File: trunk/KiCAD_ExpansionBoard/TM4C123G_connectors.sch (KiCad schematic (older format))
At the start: 22 parts, among them J1 TI_BOOSTER_40_J1, J2 TI_BOOSTER_40_J2, J3 TI_BOOSTER_40_J3, J4 TI_BOOSTER_40_J4, P10 EB_GPIO0, P6 CAN, P7 UART1, P8 RS485, P9 UART2, Q2 TSM3457

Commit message: Eliminata R8 e collegata la piazzola P1 direttamente al pin 2 del RFM23B. Schema elettrico alla versione 0.3.3 Cretata la BOM definitiva in (TM4C123G_CommExpBoard_BOM.xlsx e TM4C123G_CommExpBoard.csv) Completato lo sbroglio del PCB con serigrafie posizionate complete di logo OHSW. PCB alla versione 0.2
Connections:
- net labels added: +5V_TLP
- net labels removed: +5V
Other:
- note removed: "BUFFERIZZA IN INGRESSO ALL'ADC--> Radc=2k5!!"
- note removed: "if order skackable 10 pins header, \nyou can remove the four I2C pins \non this header (EB_GPIO0)"
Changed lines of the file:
@@
 Sheet 3 3
 Title "TM4C123G Communication Expansion Board"
-Date "15 jul 2014"
-Rev "0.3.1"
+Date "5 aug 2014"
+Rev "0.3.3"
 Comp "Luca Buccolini, Student @ Università Politecnica delle Marche"
 Comment1 "Expansion Board for the Texas Instruments TM4C123G Launchpad "
@@
 $EndComp
 $Comp
-L GND #PWR028
+L GND #PWR026
 U 1 1 53963620
 P 2550 1250
-F 0 "#PWR028" H 2550 1250 30  0001 C CNN
+F 0 "#PWR026" H 2550 1250 30  0001 C CNN
 F 1 "GND" H 2550 1180 30  0001 C CNN
 F 2 "" H 2550 1250 60  0000 C CNN
@@
 UART2_RST
 $Comp
-L GND #PWR029
+L GND #PWR027
 U 1 1 53963AEB
 P 5500 1250
-F 0 "#PWR029" H 5500 1250 30  0001 C CNN
+F 0 "#PWR027" H 5500 1250 30  0001 C CNN
 F 1 "GND" H 5500 1180 30  0001 C CNN
 F 2 "" H 5500 1250 60  0000 C CNN
@@
 SW1
 $Comp
-L GND #PWR030
+L GND #PWR028
 U 1 1 5396B38B
 P 9050 2550
-F 0 "#PWR030" H 9050 2550 30  0001 C CNN
+F 0 "#PWR028" H 9050 2550 30  0001 C CNN
 F 1 "GND" H 9050 2480 30  0001 C CNN
 F 2 "" H 9050 2550 60  0000 C CNN
@@
 $EndComp
 $Comp
-L GND #PWR031
+L GND #PWR029
 U 1 1 5396B419
 P 8800 3950
-F 0 "#PWR031" H 8800 3950 30  0001 C CNN
+F 0 "#PWR029" H 8800 3950 30  0001 C CNN
 F 1 "GND" H 8800 3880 30  0001 C CNN
 F 2 "" H 8800 3950 60  0000 C CNN
@@
 NoConn ~ 9250 6600
 $Comp
-L GND #PWR032
+L GND #PWR030
 U 1 1 5396D342
 P 1150 7300
-F 0 "#PWR032" H 1150 7300 30  0001 C CNN
+F 0 "#PWR030" H 1150 7300 30  0001 C CNN
 F 1 "GND" H 1150 7230 30  0001 C CNN
 F 2 "" H 1150 7300 60  0000 C CNN
@@
 $EndComp
 $Comp
-L GND #PWR033
+L GND #PWR031
 U 1 1 5396DC3C
 P 1450 7300
-F 0 "#PWR033" H 1450 7300 30  0001 C CNN
+F 0 "#PWR031" H 1450 7300 30  0001 C CNN
 F 1 "GND" H 1450 7230 30  0001 C CNN
 F 2 "" H 1450 7300 60  0000 C CNN
@@
 Text HLabel 3350 3250 2    60   Input ~ 0
 RS485_B
+Text HLabel 1550 3250 2    60   Input ~ 0
+CAN_H
 Text HLabel 1550 3150 2    60   Input ~ 0
-CAN_H
-Text HLabel 1550 3250 2    60   Input ~ 0
 CAN_L
 Text HLabel 9250 4500 0    60   Output ~ 0
@@
 UART3_TX
 $Comp
-L +12V_BUS #PWR034
+L +12V_BUS #PWR032
 U 1 1 5399D0A5
 P 1150 6000
-F 0 "#PWR034" H 1150 5950 20  0001 C CNN
+F 0 "#PWR032" H 1150 5950 20  0001 C CNN
 F 1 "+12V_BUS" H 1150 6100 30  0000 C CNN
 F 2 "" H 1150 6000 60  0000 C CNN
@@
 $EndComp
 $Comp
-L +12V_BUS #PWR035
+L +12V_BUS #PWR033
 U 1 1 5399D2FF
 P 3350 4450
-F 0 "#PWR035" H 3350 4400 20  0001 C CNN
+F 0 "#PWR033" H 3350 4400 20  0001 C CNN
 F 1 "+12V_BUS" H 3350 4550 30  0000 C CNN
 F 2 "" H 3350 4450 60  0000 C CNN
@@
 $EndComp
 $Comp
-L GND #PWR036
+L GND #PWR034
 U 1 1 5399D305
 P 1600 3450
-F 0 "#PWR036" H 1600 3450 30  0001 C CNN
+F 0 "#PWR034" H 1600 3450 30  0001 C CNN
 F 1 "GND" H 1600 3380 30  0001 C CNN
 F 2 "" H 1600 3450 60  0000 C CNN
@@
 $EndComp
 $Comp
-L GND #PWR037
+L GND #PWR035
 U 1 1 5399D30B
 P 3400 3450
-F 0 "#PWR037" H 3400 3450 30  0001 C CNN
+F 0 "#PWR035" H 3400 3450 30  0001 C CNN
 F 1 "GND" H 3400 3380 30  0001 C CNN
 F 2 "" H 3400 3450 60  0000 C CNN
@@
 	3650 6200 3650 6250
 $Comp
-L GND #PWR038
+L GND #PWR036
 U 1 1 539C609B
 P 3650 6750
-F 0 "#PWR038" H 3650 6750 30  0001 C CNN
+F 0 "#PWR036" H 3650 6750 30  0001 C CNN
 F 1 "GND" H 3650 6680 30  0001 C CNN
 F 2 "" H 3650 6750 60  0000 C CNN
@@
 	3650 7000 3650 7050
 $Comp
-L GND #PWR039
+L GND #PWR037
 U 1 1 539C6276
 P 3650 7550
-F 0 "#PWR039" H 3650 7550 30  0001 C CNN
+F 0 "#PWR037" H 3650 7550 30  0001 C CNN
 F 1 "GND" H 3650 7480 30  0001 C CNN
 F 2 "" H 3650 7550 60  0000 C CNN
@@
 Text HLabel 9250 4300 0    60   Input ~ 0
 RFM_CLK
-Text Notes 5750 3500 0    60   ~ 0
-if order skackable 10 pins header, \nyou can remove the four I2C pins \non this header (EB_GPIO0)
 Text Notes 2800 2750 0    60   ~ 0
 RS-485 connector &\npower supply rail
@@
 	2300 5000 2300 5050
 $Comp
-L GND #PWR040
+L GND #PWR038
 U 1 1 53A0D0E7
 P 2300 5050
-F 0 "#PWR040" H 2300 5050 30  0001 C CNN
+F 0 "#PWR038" H 2300 5050 30  0001 C CNN
 F 1 "GND" H 2300 4980 30  0001 C CNN
 F 2 "" H 2300 5050 60  0000 C CNN
@@
 	3000 5050 3000 4850
 $Comp
-L GND #PWR041
+L GND #PWR039
 U 1 1 53A176A3
 P 3000 5050
-F 0 "#PWR041" H 3000 5050 30  0001 C CNN
+F 0 "#PWR039" H 3000 5050 30  0001 C CNN
 F 1 "GND" H 3000 4980 30  0001 C CNN
 F 2 "" H 3000 5050 60  0000 C CNN
@@
 $EndComp
 $Comp
-L GND #PWR042
+L GND #PWR040
 U 1 1 53B31717
 P 6900 2850
-F 0 "#PWR042" H 6900 2850 30  0001 C CNN
+F 0 "#PWR040" H 6900 2850 30  0001 C CNN
 F 1 "GND" H 6900 2780 30  0001 C CNN
 F 2 "" H 6900 2850 60  0000 C CNN
@@
 	5950 3300 5550 3300
 $Comp
-L +3.3V #PWR043
+L +3.3V #PWR041
 U 1 1 53B3C4A0
 P 5550 6450
-F 0 "#PWR043" H 5550 6410 30  0001 C CNN
+F 0 "#PWR041" H 5550 6410 30  0001 C CNN
 F 1 "+3.3V" H 5550 6560 30  0000 C CNN
 F 2 "~" H 5550 6450 60  0000 C CNN
@@
 $EndComp
 $Comp
-L +3.3V #PWR044
+L +3.3V #PWR042
 U 1 1 53B3C4B7
 P 3000 1500
-F 0 "#PWR044" H 3000 1460 30  0001 C CNN
+F 0 "#PWR042" H 3000 1460 30  0001 C CNN
 F 1 "+3.3V" H 3000 1610 30  0000 C CNN
 F 2 "~" H 3000 1500 60  0000 C CNN
@@
 $EndComp
 $Comp
-L +3.3V #PWR045
+L +3.3V #PWR043
 U 1 1 53B3C4C7
 P 5950 1500
-F 0 "#PWR045" H 5950 1460 30  0001 C CNN
+F 0 "#PWR043" H 5950 1460 30  0001 C CNN
 F 1 "+3.3V" H 5950 1610 30  0000 C CNN
 F 2 "~" H 5950 1500 60  0000 C CNN
@@
 $EndComp
 $Comp
-L +3.3V #PWR046
+L +3.3V #PWR044
 U 1 1 53B3C4CD
 P 9050 800
-F 0 "#PWR046" H 9050 760 30  0001 C CNN
+F 0 "#PWR044" H 9050 760 30  0001 C CNN
 F 1 "+3.3V" H 9050 910 30  0000 C CNN
 F 2 "~" H 9050 800 60  0000 C CNN
@@
 $EndComp
 $Comp
-L +3.3V #PWR047
+L +3.3V #PWR045
 U 1 1 53B3C4E8
 P 5850 2850
-F 0 "#PWR047" H 5850 2810 30  0001 C CNN
+F 0 "#PWR045" H 5850 2810 30  0001 C CNN
 F 1 "+3.3V" H 5850 2960 30  0000 C CNN
 F 2 "~" H 5850 2850 60  0000 C CNN
@@
 Wire Wire Line
 	9050 4100 9050 4000
-$Comp
-L +5V #PWR048
-U 1 1 53B43EA6
-P 9050 4000
-F 0 "#PWR048" H 9050 4090 20  0001 C CNN
-F 1 "+5V" H 9050 4090 30  0000 C CNN
-F 2 "~" H 9050 4000 60  0000 C CNN
-F 3 "~" H 9050 4000 60  0000 C CNN
-	1    9050 4000
-	1    0    0    -1
-$EndComp
 $Comp
 L BID_TVS TVS3
@@
 	1    0    0    -1
 $EndComp
-Text Notes 350  6800 0    60   ~ 0
-BUFFERIZZA IN INGRESSO ALL'ADC--> Radc=2k5!!
+$Comp
+L +5V_TLP #PWR046
+U 1 1 53D830B3
+P 9050 4000
+F 0 "#PWR046" H 9050 4090 20  0001 C CNN
+F 1 "+5V_TLP" H 9050 4090 30  0000 C CNN
+F 2 "~" H 9050 4000 60  0000 C CNN
+F 3 "~" H 9050 4000 60  0000 C CNN
+	1    9050 4000
+	1    0    0    -1
+$EndComp
 $EndSCHEMATC

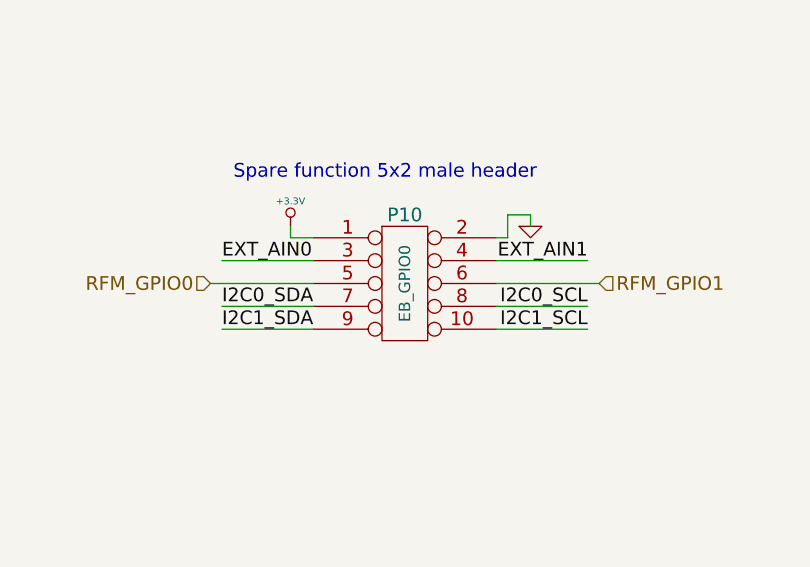
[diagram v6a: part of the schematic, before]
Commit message: Modificato il nome di P10 GPIO0 al posto di EB_GPIO0 e schematico rinominato in rev.0.3.4; di conseguenza è stato rinominato il valore di P10 anche sul PCB. Aggiornate le serigrafie dei connettori sul PCB. Aggiornato il nome della rev. sul PCB alla rev 0.4
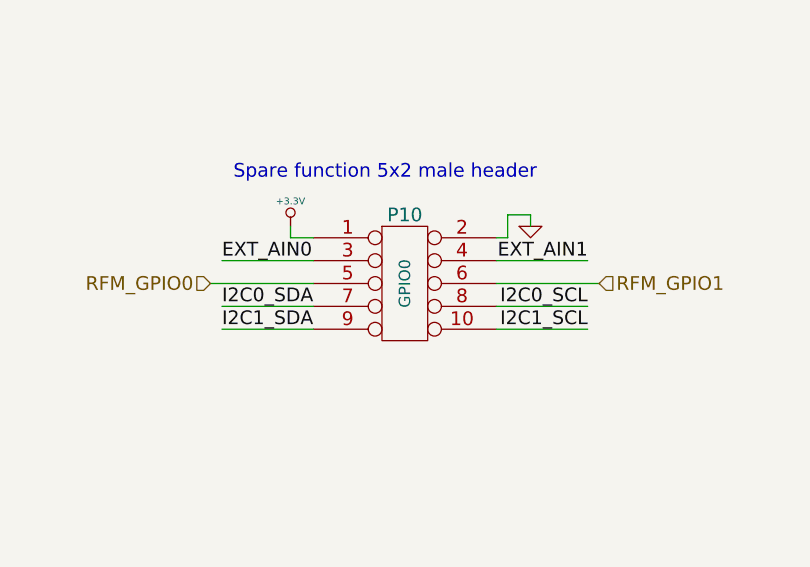
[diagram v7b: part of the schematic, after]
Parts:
- P10: value EB_GPIO0 -> GPIO0
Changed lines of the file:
@@
 Sheet 3 3
 Title "TM4C123G Communication Expansion Board"
-Date "5 aug 2014"
-Rev "0.3.3"
+Date "6 aug 2014"
+Rev "0.3.4"
 Comp "Luca Buccolini, Student @ Università Politecnica delle Marche"
 Comment1 "Expansion Board for the Texas Instruments TM4C123G Launchpad "
@@
 P 6350 3100
 F 0 "P10" H 6350 3400 60  0000 C CNN
-F 1 "EB_GPIO0" V 6350 3100 50  0000 C CNN
+F 1 "GPIO0" V 6350 3100 50  0000 C CNN
 F 2 "~" H 6350 3100 60  0001 C CNN
 F 3 "http://www.farnell.com/datasheets/1697536.pdf" H 6350 3100 60  0001 C CNN
